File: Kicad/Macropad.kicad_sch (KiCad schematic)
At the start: 86 parts, among them J1 UJ20-C-H-G-SMT-5-P16-TR, SW1 SW_SPST, SW10 SW_SPST, SW11 SW_SPST, SW12 SW_SPST, SW13 SW_SPST, SW14 SW_SPST, SW15 SW_SPST, SW16 SW_SPST, SW17 SW_SPST, SW18 SW_SPST, SW19 SW_SPST, SW2 SW_SPST, SW20 SW_SPST, SW21 SW_SPST, SW22 SW_SPST, SW23 SW_SPST, SW24 SW_SPST, SW25 SW_SPST, SW26 SW_Reset, SW27 SW_HWB, SW3 SW_SPST, SW4 SW_SPST, SW5 SW_SPST, SW6 SW_SPST, SW7 SW_SPST, SW8 SW_SPST, SW9 SW_SPST, U1 ATmega32U4-A, Y1 LFXTAL085842

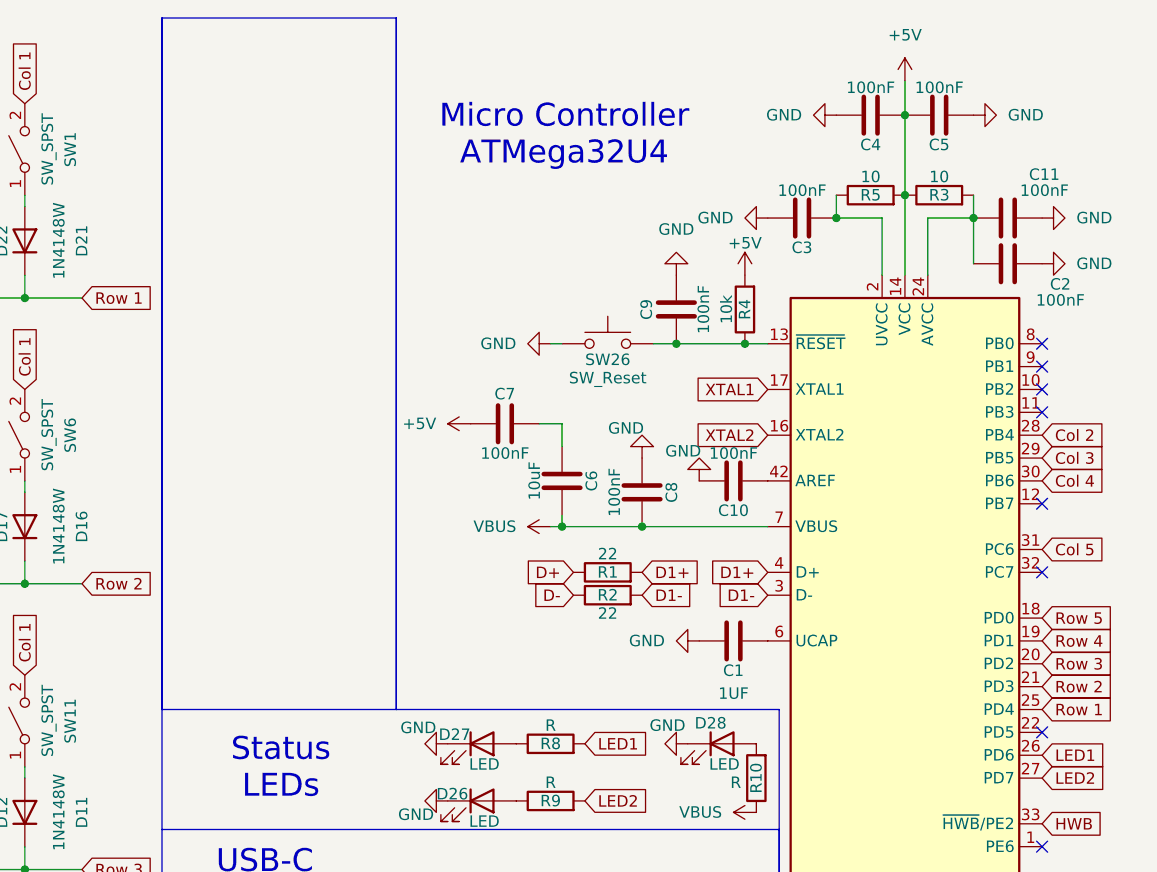
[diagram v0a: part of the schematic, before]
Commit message: added debug pins
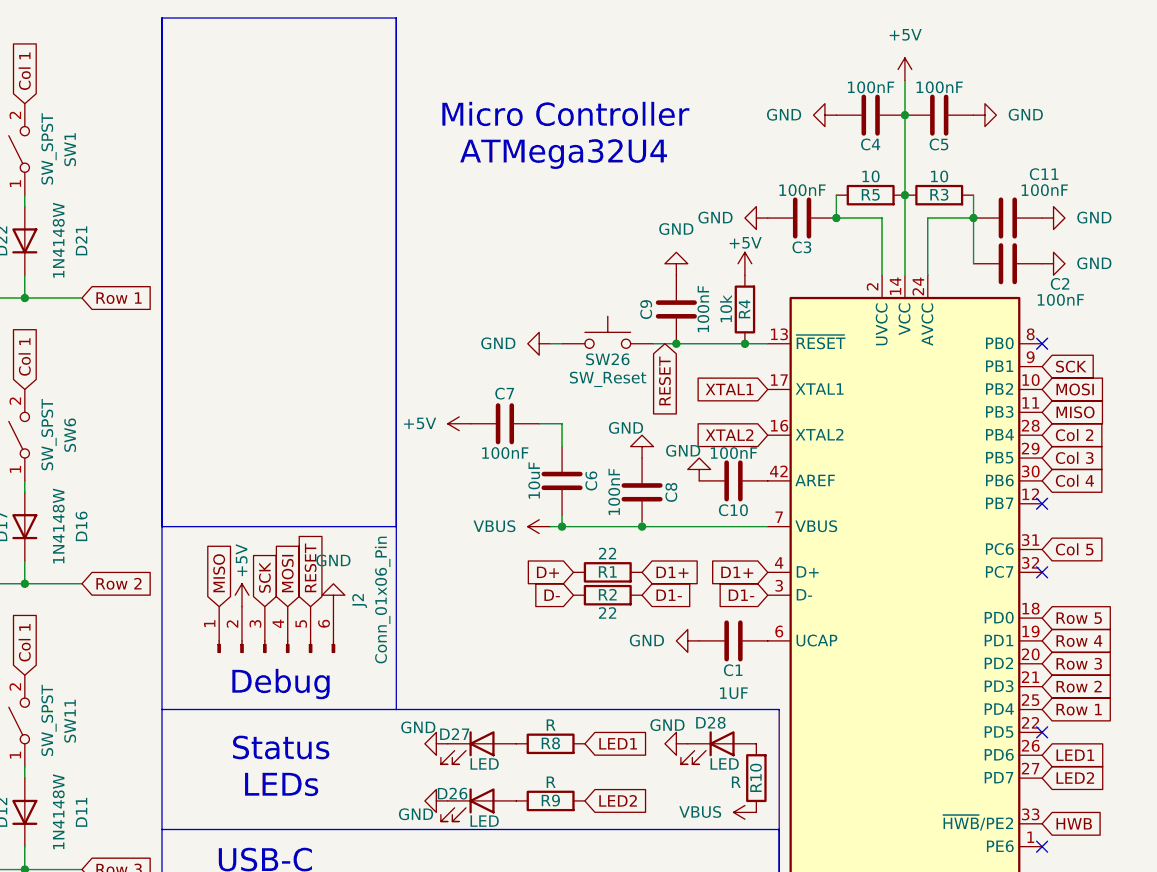
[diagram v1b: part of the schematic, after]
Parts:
- added J2: Conn_01x06_Pin, Connector_PinHeader_2.54mm:PinHeader_2x03_P2.54mm_Vertical, symbol Connector:Conn_01x06_Pin
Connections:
- net +5V: now also J2.2 (Pin_2)
- net GND: now also J2.6 (Pin_6)
- net RESET: now reaches C9.1, R4.1, SW26.2, U1.13 (~{RESET})
- net RESET: now also J2.5 (Pin_5)
- net MOSI: now reaches U1.10 (PB2)
- net MOSI: now also J2.4 (Pin_4)
- net MISO: now reaches U1.11 (PB3)
- net MISO: now also J2.1 (Pin_1)
- net SCK: now reaches U1.9 (PB1)
- net SCK: now also J2.3 (Pin_3)
- no-connect marks 15 -> 12
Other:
- note added: "Debug"
